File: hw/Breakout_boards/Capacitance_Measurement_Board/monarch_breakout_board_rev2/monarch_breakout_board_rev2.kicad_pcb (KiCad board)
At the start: 2 copper layers, 24.6 x 27.1 mm, 42 parts, among them J1 Conn_01x02, J2 Conn_01x02, J3 Conn_01x02, J4 Conn_01x02, J9 2200980471, U1 FDC2214RGHR

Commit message: I2C
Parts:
- moved C22 63.7 mm to (117.2, 57.0), turned to 180 degrees
- moved C21 62.1 mm to (117.2, 58.5)
- moved SDA 37.0 mm to (109.9, 54.4)
- moved 3V3 17.0 mm to (113.2, 62.2)
- moved SCL 14.2 mm to (109.9, 49.9)
- moved J9 0.50 mm to (117.0, 61.1)
- renumbered TP3 to 3V3, TP1 to SCL, TP4 to SDA
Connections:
- U1 pad V: (no net) -> GND
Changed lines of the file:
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@@
 	(footprint "TestPoint:TestPoint_Keystone_5000-5004_Miniature"
 		(layer "F.Cu")
-		(at 95.7 50.3 180)
+		(at 109.9 49.85 180)
 		(descr "Keystone THM Miniature Test Point 5000-5004, http://www.keyelco.com/product-pdf.cfm?p=1309")
 		(tags "Through Hole Mount Test Points")
-		(property "Reference" "TP1"
+		(property "Reference" "SCL"
 			(at 0.025 2.4 0)
 			(layer "F.SilkS")
@@
 	(footprint "Capacitor_SMD:C_0603_1608Metric"
 		(layer "F.Cu")
-		(at 174.375 82.685)
+		(at 117.22548 58.487005)
 		(descr "Capacitor SMD 0603 (1608 Metric), square (rectangular) end terminal, IPC-7351 nominal, (Body size source: IPC-SM-782 page 76, https://www.pcb-3d.com/wordpress/wp-content/uploads/ipc-sm-782a_amendment_1_and_2.pdf)")
 		(tags "capacitor")
 		(property "Reference" "C21"
-			(at 0 -1.43 0)
+			(at -2.87548 -0.087005 0)
 			(layer "F.SilkS")
 			(effects
@@
 			(layers "*.Cu" "*.Mask")
 			(remove_unused_layers no)
+			(net "GND")
 		)
 		(pad "V" thru_hole circle
@@
 			(layers "*.Cu" "*.Mask")
 			(remove_unused_layers no)
+			(net "GND")
 		)
 		(pad "V" thru_hole circle
@@
 			(layers "*.Cu" "*.Mask")
 			(remove_unused_layers no)
+			(net "GND")
 		)
 		(pad "V" thru_hole circle
@@
 			(layers "*.Cu" "*.Mask")
 			(remove_unused_layers no)
+			(net "GND")
 		)
 		(pad "V" thru_hole circle
@@
 			(layers "*.Cu" "*.Mask")
 			(remove_unused_layers no)
+			(net "GND")
 		)
 		(embedded_fonts no)
@@
 	(footprint "TestPoint:TestPoint_Keystone_5000-5004_Miniature"
 		(layer "F.Cu")
-		(at 144.6 67.2 180)
+		(at 109.9 54.4 180)
 		(descr "Keystone THM Miniature Test Point 5000-5004, http://www.keyelco.com/product-pdf.cfm?p=1309")
 		(tags "Through Hole Mount Test Points")
-		(property "Reference" "TP4"
-			(at 2.725 0.05 0)
+		(property "Reference" "SDA"
+			(at 0.1 2.15 0)
 			(layer "F.SilkS")
 			(effects
@@
 	(footprint "Connector_Molex_Micro-Lock-Plus:Molex_Micro-Lock_2200980471_1x04_P1.25mm_Horizontal"
 		(layer "F.Cu")
-		(at 117.5354 61.076201)
+		(at 117.0354 61.126201)
 		(tags "2200980471 ")
 		(property "Reference" "J9"
@@
 	(footprint "TestPoint:TestPoint_Keystone_5000-5004_Miniature"
 		(layer "F.Cu")
-		(at 97.05 56.95 180)
+		(at 113.2 62.2 180)
 		(descr "Keystone THM Miniature Test Point 5000-5004, http://www.keyelco.com/product-pdf.cfm?p=1309")
 		(tags "Through Hole Mount Test Points")
-		(property "Reference" "TP3"
+		(property "Reference" "3V3"
 			(at -0.1 -2.475 0)
 			(layer "F.SilkS")
@@
 	(footprint "Capacitor_SMD:C_0603_1608Metric"
 		(layer "F.Cu")
-		(at 174.375 85.195)
+		(at 117.225 56.95 180)
 		(descr "Capacitor SMD 0603 (1608 Metric), square (rectangular) end terminal, IPC-7351 nominal, (Body size source: IPC-SM-782 page 76, https://www.pcb-3d.com/wordpress/wp-content/uploads/ipc-sm-782a_amendment_1_and_2.pdf)")
 		(tags "capacitor")
 		(property "Reference" "C22"
-			(at 0 -1.43 0)
+			(at 2.975 0 0)
 			(layer "F.SilkS")
 			(effects
@@
 		(duplicate_pad_numbers_are_jumpers no)
 		(fp_line
-			(start -0.14058 -0.51)
-			(end 0.14058 -0.51)
+			(start -0.14058 0.51)
+			(end 0.14058 0.51)
 			(stroke
 				(width 0.12)
@@
 		)
 		(fp_line
-			(start -0.14058 0.51)
-			(end 0.14058 0.51)
+			(start -0.14058 -0.51)
+			(end 0.14058 -0.51)
 			(stroke
 				(width 0.12)
@@
 		)
 		(pad "1" smd roundrect
-			(at -0.775 0)
+			(at -0.775 0 180)
 			(size 0.9 0.95)
 			(layers "F.Cu" "F.Mask" "F.Paste")
@@
 		)
 		(pad "2" smd roundrect
-			(at 0.775 0)
+			(at 0.775 0 180)
 			(size 0.9 0.95)
 			(layers "F.Cu" "F.Mask" "F.Paste")
@@
 		(layer "B.Cu")
 		(hatch edge 0.5)
-		(priority 1)
 		(connect_pads yes
 			(clearance 0)
@@
 		(polygon
 			(pts
-				(xy 130.8 67.4) (xy 130.7 38.125) (xy 106.275 38.175) (xy 106.425 67.4)
+				(xy 124.5 66.3) (xy 124.5 60.35) (xy 120.7 60.35) (xy 120.65 49.95) (xy 111.7 49.95) (xy 111.7 38)
+				(xy 105.45 38) (xy 105.45 66.3)
 			)
 		)

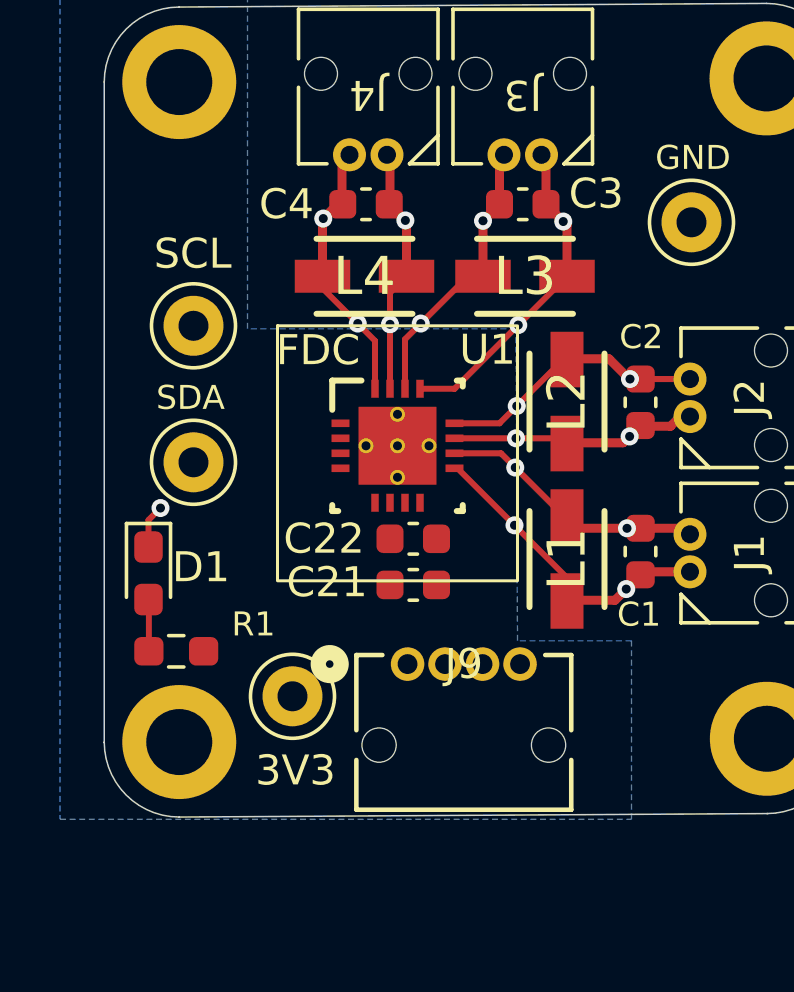
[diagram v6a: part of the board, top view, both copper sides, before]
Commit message: Back Layer Noise Caps Placed
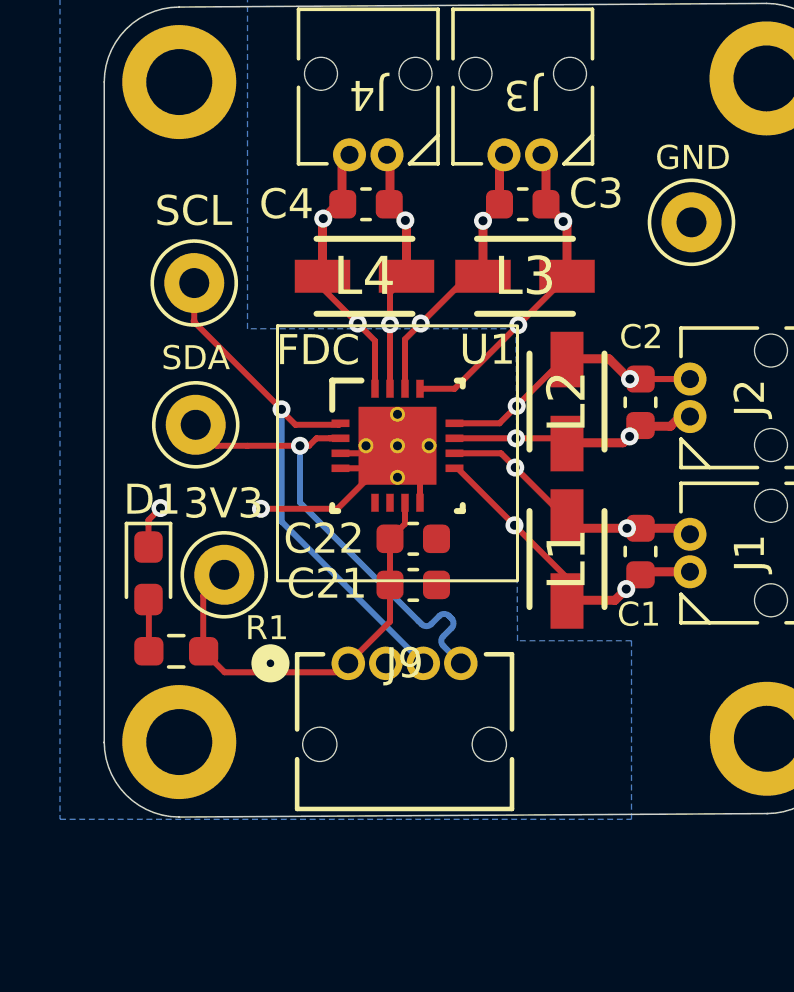
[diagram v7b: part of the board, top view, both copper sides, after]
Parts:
- moved 3V3 4.65 mm to (110.9, 58.1)
- moved J9 1.98 mm to (115.1, 61.1)
- moved SCL 1.43 mm to (109.9, 48.4)
- moved SDA 1.25 mm to (110.0, 53.1)
- turned C21 to 180 degrees
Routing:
- net /I2C4_SCL: track 0.00 -> 18.1 mm, vias 0 -> 1
- net /I2C4_SDA: track 0.00 -> 15.9 mm, vias 0 -> 1
- net +3V3: track 0.04 -> 14.3 mm
- net GND: track 1.47 -> 13.4 mm, vias 1 -> 2

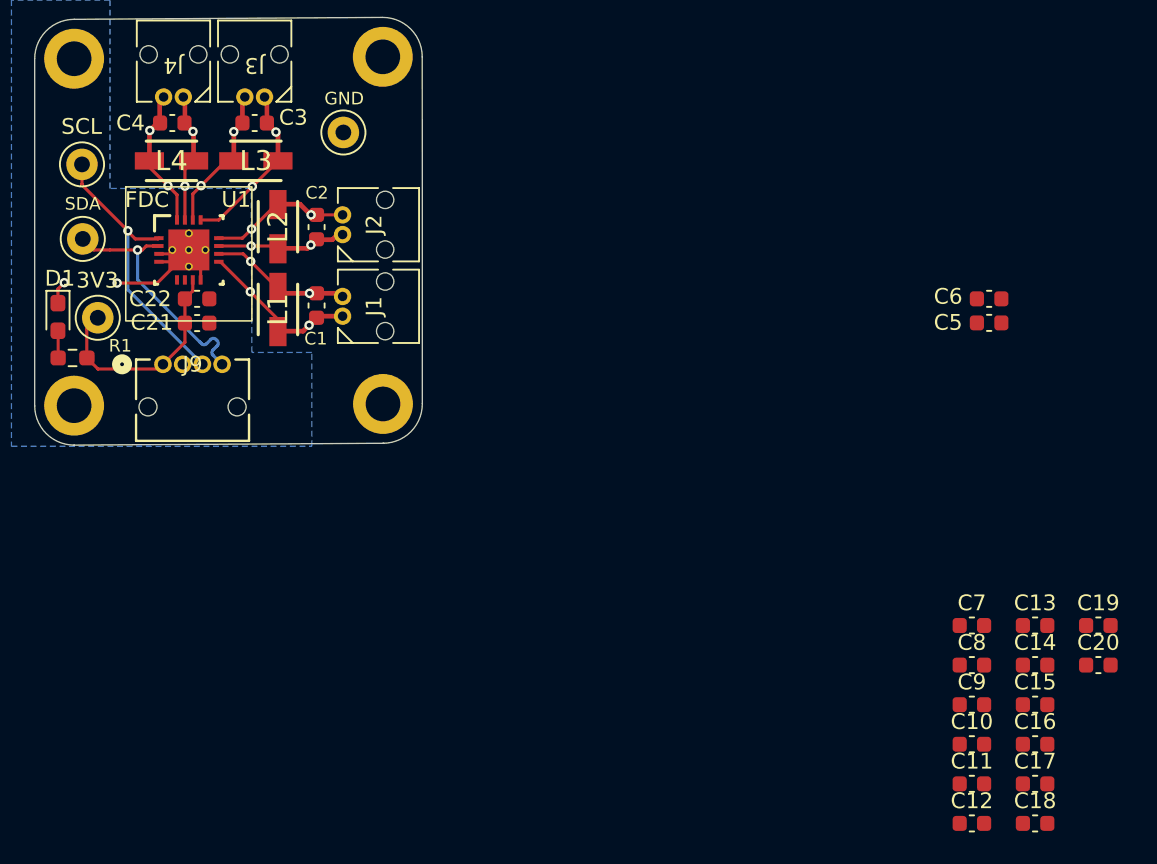
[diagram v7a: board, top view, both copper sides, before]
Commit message: Back Layer Routing Done
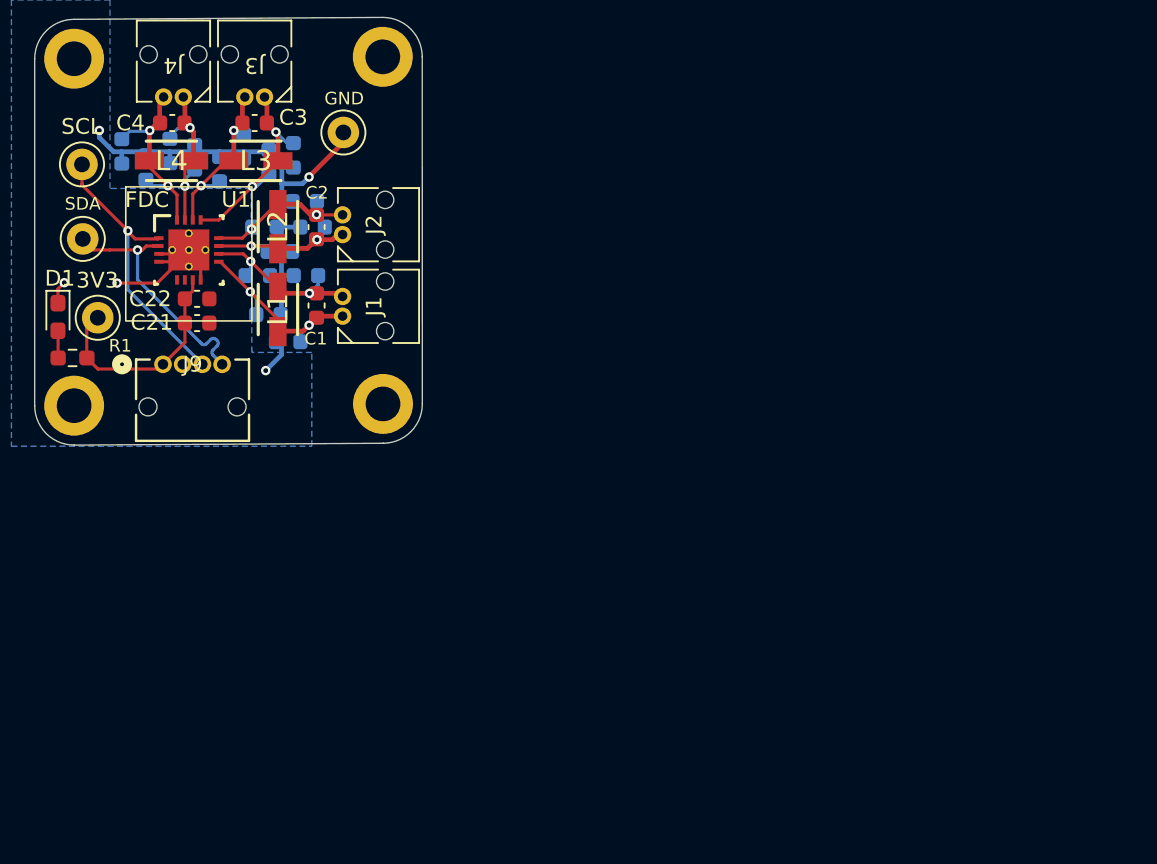
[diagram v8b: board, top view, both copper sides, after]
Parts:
- C10, C11, C12, C13, C14, C15, C16, C17, C18, C19, C20, C5, C6, C7, C8, C9: moved to B.Cu
- moved C12 68.7 mm to (112.5, 47.6), turned to 90 degrees
- moved C20 68.1 mm to (114.0, 48.6), turned to -90 degrees
- moved C18 66.3 mm to (118.7, 48.7), turned to -90 degrees
- moved C11 64.8 mm to (115.5, 47.6), turned to -90 degrees
- moved C19 64.5 mm to (117.1, 48.0), turned to 90 degrees
- moved C17 62.6 mm to (121.8, 48.3), turned to 90 degrees
- moved C10 59.7 mm to (120.2, 47.3), turned to 90 degrees
- moved C16 57.6 mm to (121.1, 55.5), turned to 180 degrees
- moved C14 56.2 mm to (121.5, 52.4), turned to 180 degrees
- moved C9 55.4 mm to (123.3, 47.9), turned to -90 degrees
- moved C15 54.5 mm to (121.8, 58.0)
- moved C13 53.4 mm to (122.5, 54.0)
- moved C8 48.9 mm to (124.1, 55.5)
- moved C7 46.9 mm to (123.0, 59.7), turned to 180 degrees
- moved C6 43.8 mm to (124.0, 50.8)
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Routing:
- net GND: track 13.4 -> 54.6 mm, vias 2 -> 5
- net /Cap3-: track 9.02 -> 12.6 mm
- net /Cap3+: track 8.32 -> 11.3 mm
- net /Cap0+: track 10.5 -> 13.4 mm
- net /Cap2+: track 10.9 -> 13.6 mm
- net /Cap0-: track 8.97 -> 11.4 mm
- net /Cap1+: track 8.32 -> 10.5 mm
- net /Cap2-: track 9.46 -> 11.5 mm
- net /Cap1-: track 9.02 -> 10.2 mm
